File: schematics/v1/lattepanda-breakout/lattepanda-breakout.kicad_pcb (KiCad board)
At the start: 4 copper layers, 39.4 x 76.2 mm, 23 parts, among them J1 Arduino, J2 Arduino, J3 COM(RS232/485), J4 Front Panel, J5 SDI12, J6 RS485, J7 RS232, J8 PiKVM, J9 RS422, U1 MAX22508, U2 TRSF3232ECD, U3 TLV75533PDBV

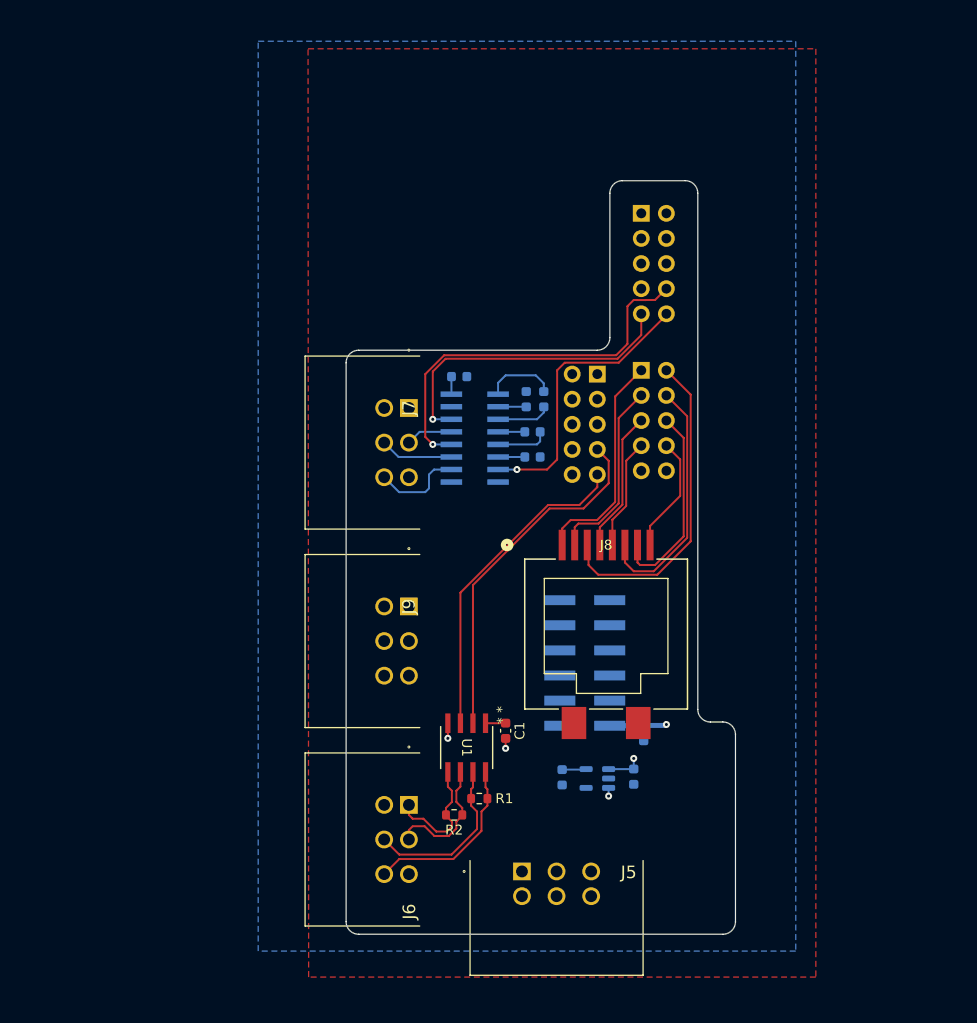
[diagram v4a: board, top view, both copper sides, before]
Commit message: Add rs422 GPS breakout to LP breakout
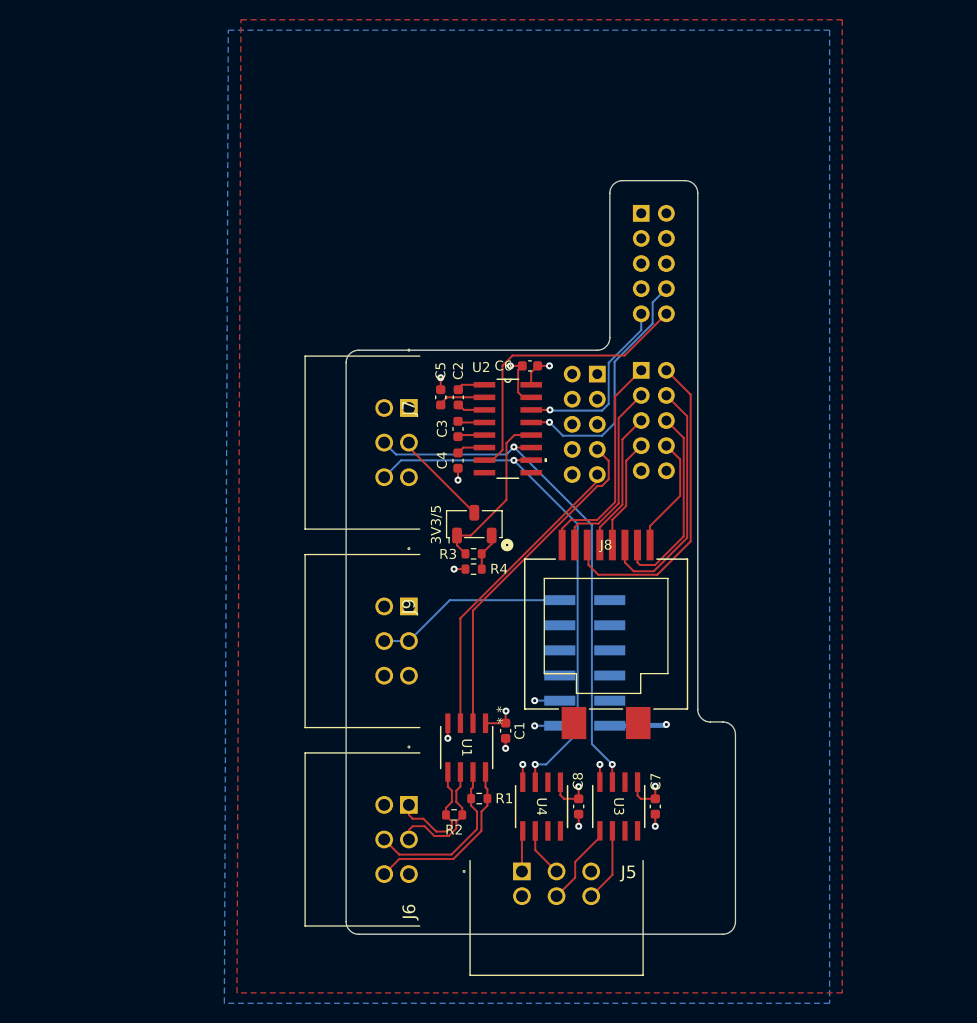
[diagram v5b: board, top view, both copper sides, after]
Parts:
- removed C9: 1uF, Capacitor_SMD:C_0603_1608Metric
- added 3V3/5: 3V3/5V, Button_Switch_SMD:Nidec_Copal_CAS-120A, F.Cu at (64.4, 66.1)
- added R3: 3.3k, Resistor_SMD:R_0603_1608Metric, F.Cu at (64.3, 69.1)
- added R4: 6.8k, Resistor_SMD:R_0603_1608Metric, F.Cu at (64.3, 70.7)
- added U4: MAX22508, Link_Footprints:MAX22508, F.Cu at (71.2, 94.7)
- C2, C3, C4, C5, C6, U2: moved to F.Cu
- C7, C8: value 1uF -> 0.1uF; moved to F.Cu
- J5: value SDI12 -> RS422
- J9: value RS422 -> SDI12
- U3: value TLV75533PDBV -> MAX22508; footprint Package_TO_SOT_SMD:SOT-23-5 -> Link_Footprints:MAX22508; moved to F.Cu
- moved C2 8.65 mm to (62.8, 53.3)
- moved C5 8.65 mm to (61.0, 53.3)
- moved C4 7.54 mm to (62.8, 59.7), turned to 90 degrees
- moved C3 7.54 mm to (62.8, 56.5), turned to -90 degrees
- moved C6 7.24 mm to (70.0, 50.1), turned to 180 degrees
- moved C7 3.72 mm to (82.7, 94.7)
- moved U3 3.56 mm to (79.0, 94.7), turned to -90 degrees
- moved U2 3.48 mm to (67.8, 56.5), turned to 0 degrees
- moved C8 3.39 mm to (75.0, 94.7)
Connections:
- C6 pad 1: +3V3 -> +5V
- C8 pad 1: +3V3 -> +5V
- J5 pad 1: +5V -> /422_PPS+
- J5 pad 2: /SDI12 -> /422_PPS-
- J5 pad 5: /SDI12 -> /422_TX+
- J5 pad 6: GND -> /422_TX-
- J9 pad 1: /422_PPS+ -> +5V
- J9 pad 2: /422_PPS- -> /SDI12
- J9 pad 5: /422_TX+ -> /SDI12
- J9 pad 6: /422_TX- -> GND
- U2 pad 12: /LP_TX -> Net-(SW1-C)
- U2 pad 13: /GPS_RX -> /LP_TX
- U2 pad 16: +3V3 -> +5V
- U3 pad 2: GND -> unconnected-(U3-RO-Pad2)
- U3 pad 3: +5V -> /GPS_TX
- U3 pad 4: unconnected-(U3-NC-Pad4) -> GND
- U3 pad 5: +3V3 -> /422_TX+
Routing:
- net /GPS_TX: track 7.39 -> 53.7 mm, vias 0 -> 2
- net /GPS_PPS: track 9.18 -> 53.2 mm, vias 0 -> 2
- net GND: track 2.53 -> 22.8 mm, vias 2 -> 12
- net /SDI12: track 0.00 -> 19.5 mm
- net Net-(SW1-C): track 0.00 -> 17.3 mm
- net /LP_TX: track 39.5 -> 25.3 mm
- net /LP_RX: track 31.5 -> 18.6 mm
- net +5V: track 12.3 -> 21.5 mm, vias 3 -> 5
- net /422_TX+: track 0.00 -> 8.42 mm
- net /422_TX-: track 0.00 -> 7.50 mm
- net /GPS_RX: track 4.74 -> 9.83 mm
- net /422_PPS-: track 0.00 -> 4.98 mm
- net Net-(U2-C1+): track 7.24 -> 2.84 mm
- net +3V3: track 4.23 -> 0.00 mm
- net /422_PPS+: track 0.00 -> 4.12 mm
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- added copper zone on In1.Cu, net +5V
- added copper zone on F.Cu, net GND
- added copper zone on In2.Cu, net GND
- removed copper zone on F.Cu, net +5V

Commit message: minor cleanup
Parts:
- moved R4 1.40 mm to (64.3, 69.2)
- moved 3V3/5 1.40 mm to (64.4, 64.7)
- moved R3 1.40 mm to (64.3, 67.7)
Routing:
- net Net-(SW1-C): track 17.3 -> 15.9 mm
- net /GPS_RX: track 9.83 -> 8.97 mm
- net GND: track 22.8 -> 22.0 mm
- net /LP_DCD: track 29.5 -> 28.7 mm
- net /485_TX: track 30.9 -> 30.2 mm
- net /422_TX+: track 8.42 -> 7.78 mm
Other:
- board text added: "3V3"
- board text added: "5V"

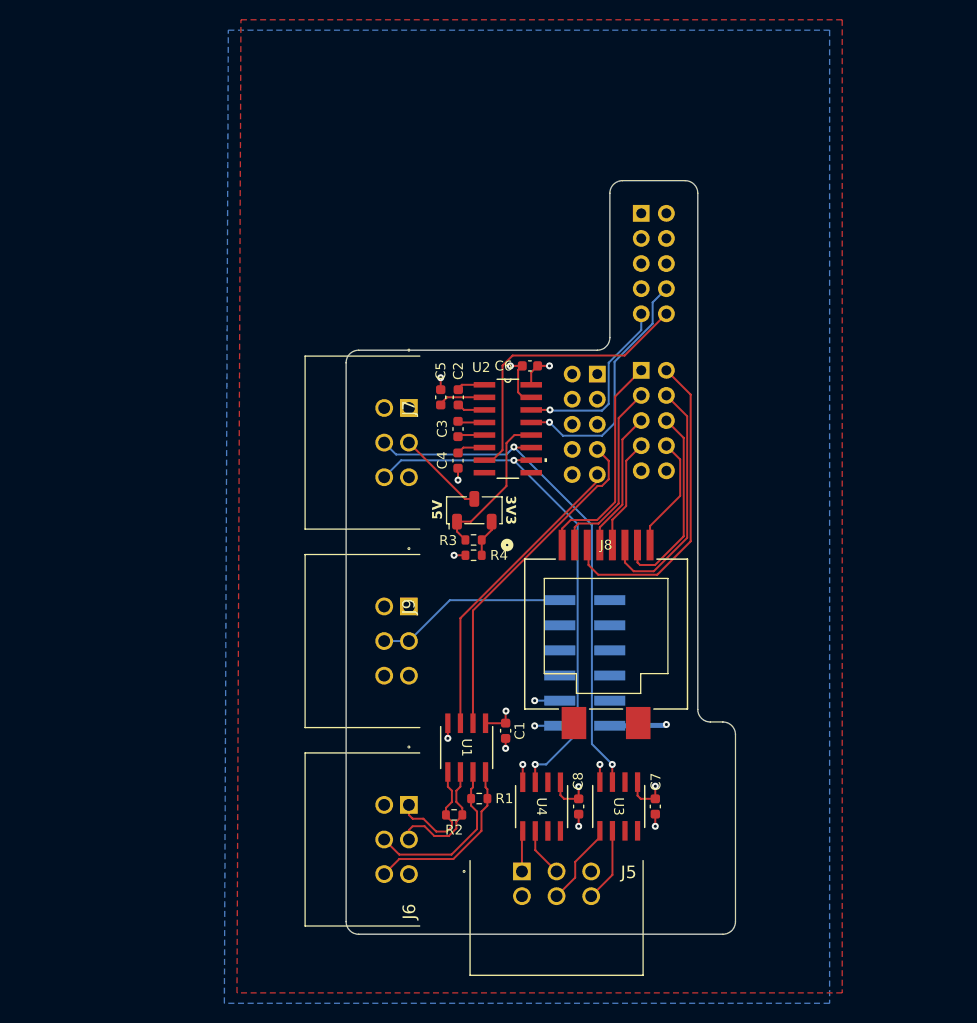
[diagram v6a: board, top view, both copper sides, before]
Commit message: complete lattepanda-breakout
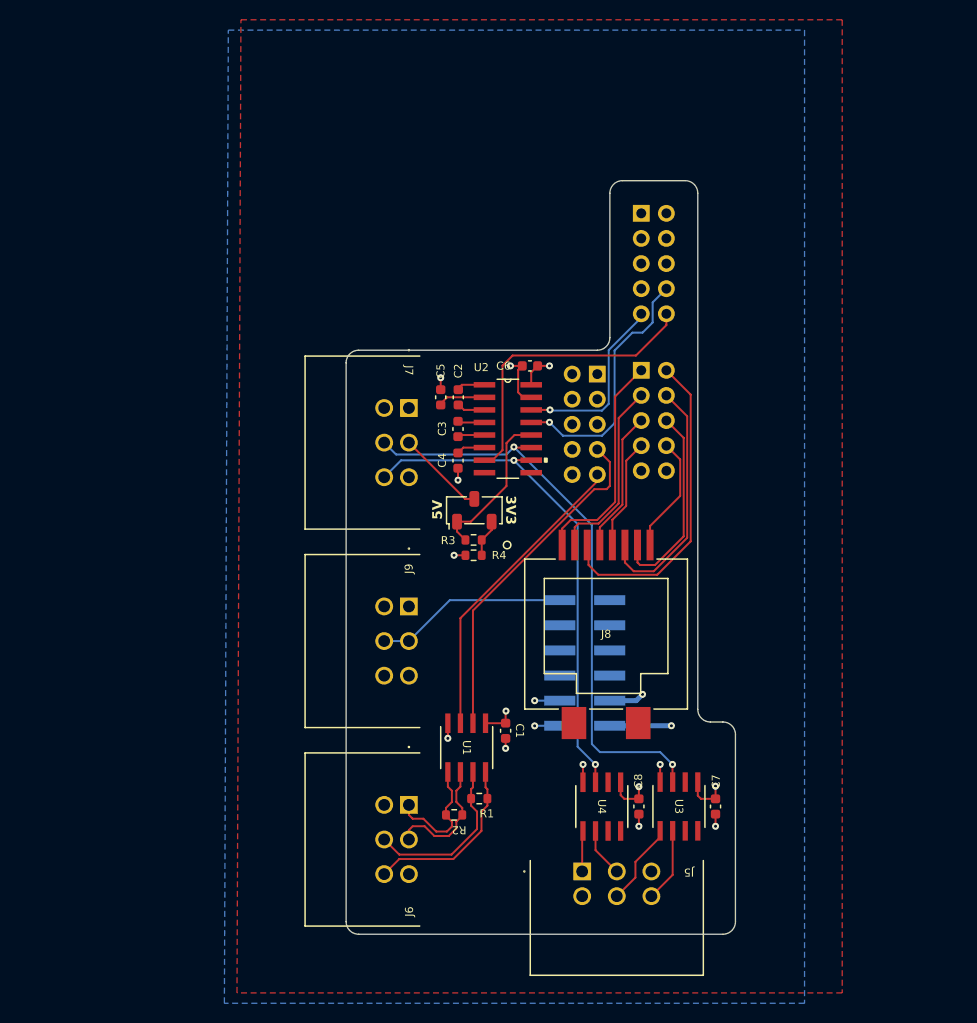
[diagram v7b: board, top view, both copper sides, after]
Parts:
- added REF**: PC-PinLabel, New_Footprints:PC-PinLabel, B.Cu at (78.9, 94.7)
- added REF**: PC-PinLabel, New_Footprints:PC-PinLabel, B.Cu at (64.4, 78.1)
- added REF**: PC-PinLabel, New_Footprints:PC-PinLabel, B.Cu at (64.3, 57.9)
- added REF**: PC-PinLabel, New_Footprints:PC-PinLabel, B.Cu at (64.4, 98.2)
- moved C7 6.09 mm to (88.8, 94.7)
- moved C8 6.09 mm to (81.0, 94.7)
- moved J5 6.09 mm to (75.3, 101.2)
- moved U3 6.09 mm to (85.1, 94.7)
- moved U4 6.09 mm to (77.3, 94.7)
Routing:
- net /GPS_TX: track 53.7 -> 59.8 mm
- net +5V: track 21.5 -> 25.6 mm, vias 5 -> 6
- net /GPS_PPS: track 53.2 -> 51.5 mm
- net /LP_DCD: track 28.7 -> 29.4 mm
- net /LP_TX: track 25.3 -> 25.9 mm
- net /485_RX: track 34.1 -> 34.7 mm

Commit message: lattepanda-breakout finish
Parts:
- REF** (x4): footprint New_Footprints:PC-PinLabel -> Link_Footprints:PC-PinLabel
- U1, U3, U4: value MAX22508 -> 21-0041_S8+2C_MXM
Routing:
- added copper zone on In2.Cu, net +5V
- added copper zone on In1.Cu, net GND
- removed copper zone on In1.Cu, net +5V
- removed copper zone on In2.Cu, net GND
